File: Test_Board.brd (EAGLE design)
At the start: 50.8 x 50.8 mm, 24 parts, among them U1 Value, U2 Value

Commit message: initial placements done
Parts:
- removed C3: (no value), SparkFun-Capacitors:0603
- removed D1: 3A/40V/500mV, SparkFun-DiscreteSemi:SMA-DIODE
- added C11: 330uF, brick-capacitor-UCM1H331MNL1GS:CAPAE1030X1050N
- added J1, J2, J3: (no value), SparkFun-Connectors:2X4
- added JP1, JP2: JUMPER-SMT_2_NO_NO-SILK, SparkFun-Jumpers:SMT-JUMPER_2_NO_NO-SILK
- added U$4: SWITCHMODE_SCHOTTKY, PowerComponents:DPAK-3
- moved R3 82.6 mm to (31.1, 22.9), turned to 270 degrees
- moved C10 77.0 mm to (27.9, 19.6), turned to 180 degrees
- moved C7 73.1 mm to (34.9, 41.9), turned to 270 degrees
- moved Q1 73.0 mm to (45.1, 40.6), turned to 270 degrees
- moved C5 67.0 mm to (31.1, 16.5), turned to 270 degrees
- moved RSEN 65.4 mm to (38.7, 50.8)
- moved L2 65.3 mm to (42.5, 17.1), turned to 270 degrees
- moved C8 64.8 mm to (24.1, 43.4), turned to 270 degrees
- moved C6 64.3 mm to (34.9, 4.45)
- moved C4 63.7 mm to (26.8, 43.4), turned to 270 degrees
- moved RFB2 60.6 mm to (26.7, 15.9), turned to 90 degrees
- moved U2 48.9 mm to (6.99, 37.5)
- moved C9 47.6 mm to (14.6, 45.3), turned to 90 degrees
- moved C2 44.7 mm to (5.71, 40.6), turned to 180 degrees
- moved U$2 44.4 mm to (10.2, 24.8), turned to 180 degrees
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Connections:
- new net N$14: JP2.2, Q1.1, Q1.2, Q1.3, RSEN.2
- net +12V: now also C11.+; no longer C3.1
- net +12V_A: now also J1.1, J1.3, J1.5, J1.7
- net +12V_B: now also J2.1, J2.3, J2.5, J2.7
- net +48V: now also J3.1, J3.3, J3.5, J3.7
- net 12V_GND: now also C11.-, J1.2, J1.4, J1.6, J1.8, J2.2, J2.4, J2.6, J2.8; no longer C3.2
- net GND: now also J3.2, J3.4, J3.6, J3.8, U$4.P$1, U$4.P$3; no longer D1.A
- net N$1: now also JP1.2, JP2.1; no longer Q1.1, Q1.2, Q1.3, RSEN.2
- net N$11: now also JP1.1, U$4.P$4; no longer D1.C
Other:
- board size 50.8 x 50.8 mm -> 63.5 x 57.1 mm

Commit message: finished routing, but dont have senior design DRC on my PC to check
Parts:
- removed C6: 100uF, SparkFun-Capacitors:EIA7343
- added C3: 150uF, PowerComponents:CTAN(7.30_4.30MM)
- added J4: (no value), SparkFun-Connectors:2X4
- moved RADJ 3.81 mm to (15.9, 45.3)
- moved U$3 3.81 mm to (15.9, 40.6)
- moved C9 3.81 mm to (18.4, 45.3)
- moved JP2 3.24 mm to (24.1, 39.4), turned to 0 degrees
- moved RT 2.54 mm to (12.2, 45.3)
- moved J3 2.54 mm to (21.6, 52.7)
- moved RFB1 1.91 mm to (16.5, 36.2)
- moved JP1 1.65 mm to (20.3, 37.7)
- moved U$4 1.27 mm to (39.4, 30.5)
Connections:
- removed net 12V_GND: C11.-, J1.2, J1.4, J1.6, J1.8, J2.2, J2.4, J2.6, J2.8
- net +12V: now also J4.1, J4.3, J4.5, J4.7
- net +5V: now also C3.+; no longer C6.A
- net GND: now also C11.-, C3.-, J1.2, J1.4, J1.6, J1.8, J2.2, J2.4, J2.6, J2.8, J4.2, J4.4, J4.6, J4.8; no longer C6.C
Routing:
- net N$11: track 0.00 -> 53.2 mm
- net N$16: track 0.00 -> 34.7 mm
- net N$14: track 0.00 -> 31.5 mm, vias 0 -> 2
- net +12V: track 0.00 -> 31.5 mm, vias 0 -> 2
- net GND: track 0.00 -> 27.5 mm, vias 0 -> 5
- net N$4: track 0.00 -> 24.6 mm
- net +48V: track 0.00 -> 14.9 mm
- net N$13: track 0.00 -> 11.2 mm
- net N$10: track 0.00 -> 10.7 mm
- net N$12: track 0.00 -> 6.65 mm
- net N$1: track 0.00 -> 6.51 mm
- net N$15: track 0.00 -> 5.60 mm
- net N$9: track 0.00 -> 4.70 mm
- net N$5: track 0.00 -> 4.70 mm
- net N$2: track 0.00 -> 4.44 mm
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- added copper zone on layer 1, net +12V
- added copper zone on layer 1, net +12V_A
- added copper zone on layer 1, net +12V_B
- added copper zone on layer 1, net +48V
- added copper zone on layer 1, net +5V
- added copper zone on layer 16, net GND
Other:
- board text added: "+12V"
- board text added: "+48V"
- board text added: "12V Out"
- board text added: "12V_A"
- board text added: "12V_B"
- board text added: "GND"

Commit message: finished routing. Need DRC
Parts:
- added J5: (no value), SparkFun-Connectors:1X04_NO_SILK
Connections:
- net +5V: now also J5.3, J5.4
- net GND: now also J5.1, J5.2
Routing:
- net GND: track 27.5 -> 28.2 mm, vias 5 -> 6
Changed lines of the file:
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@@
 <attribute name="VALUE" x="0.635" y="8.763" size="0.6096" layer="27" font="vector" ratio="20" rot="R180"/>
+</element>
+<element name="J5" library="SparkFun-Connectors" library_urn="urn:adsk.eagle:library:513" package="1X04_NO_SILK" package3d_urn="urn:adsk.eagle:package:38094/1" value="" x="40.005" y="2.54" smashed="yes">
+<attribute name="NAME" x="38.735" y="3.937" size="0.6096" layer="25" font="vector" ratio="20"/>
+<attribute name="PROD_ID" value="CONN-09696" x="40.005" y="2.54" size="1.778" layer="27" display="off"/>
+<attribute name="VALUE" x="38.735" y="0.508" size="0.6096" layer="27" font="vector" ratio="20"/>
 </element>
 </elements>
@@
 <contactref element="J4" pad="6"/>
 <contactref element="J4" pad="4"/>
-<wire x1="17.36" y1="36.195" x2="15.875" y2="40.64" width="0" layer="19" extent="1-1"/>
+<contactref element="J5" pad="1"/>
+<contactref element="J5" pad="2"/>
+<wire x1="15.875" y1="40.64" x2="15.875" y2="40.005" width="0.508" layer="1"/>
+<via x="15.875" y="40.005" extent="1-16" drill="0.35"/>
 </signal>
 <signal name="+5V">
@@
 <vertex x="31.75" y="7.62"/>
 </polygon>
+<contactref element="J5" pad="3"/>
+<contactref element="J5" pad="4"/>
 </signal>
 <signal name="+48V">

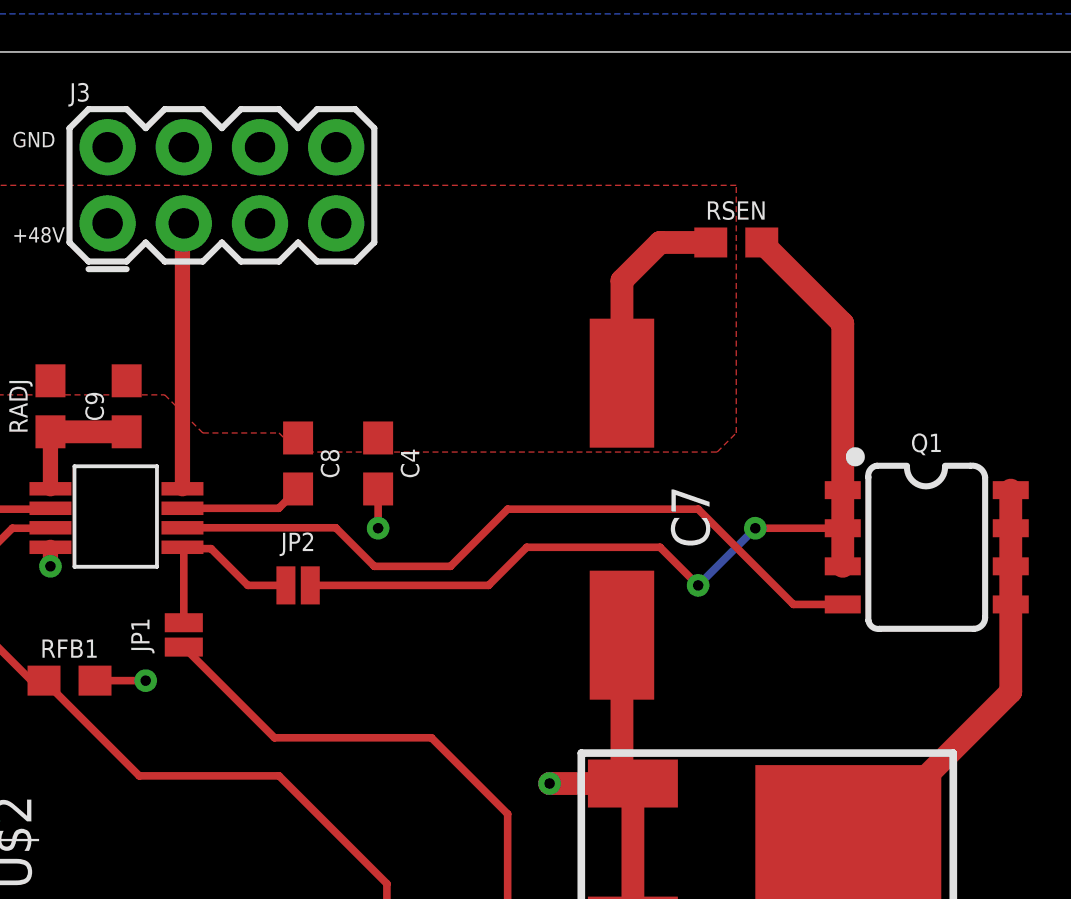
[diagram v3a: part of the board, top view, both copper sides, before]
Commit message: added sense resistor
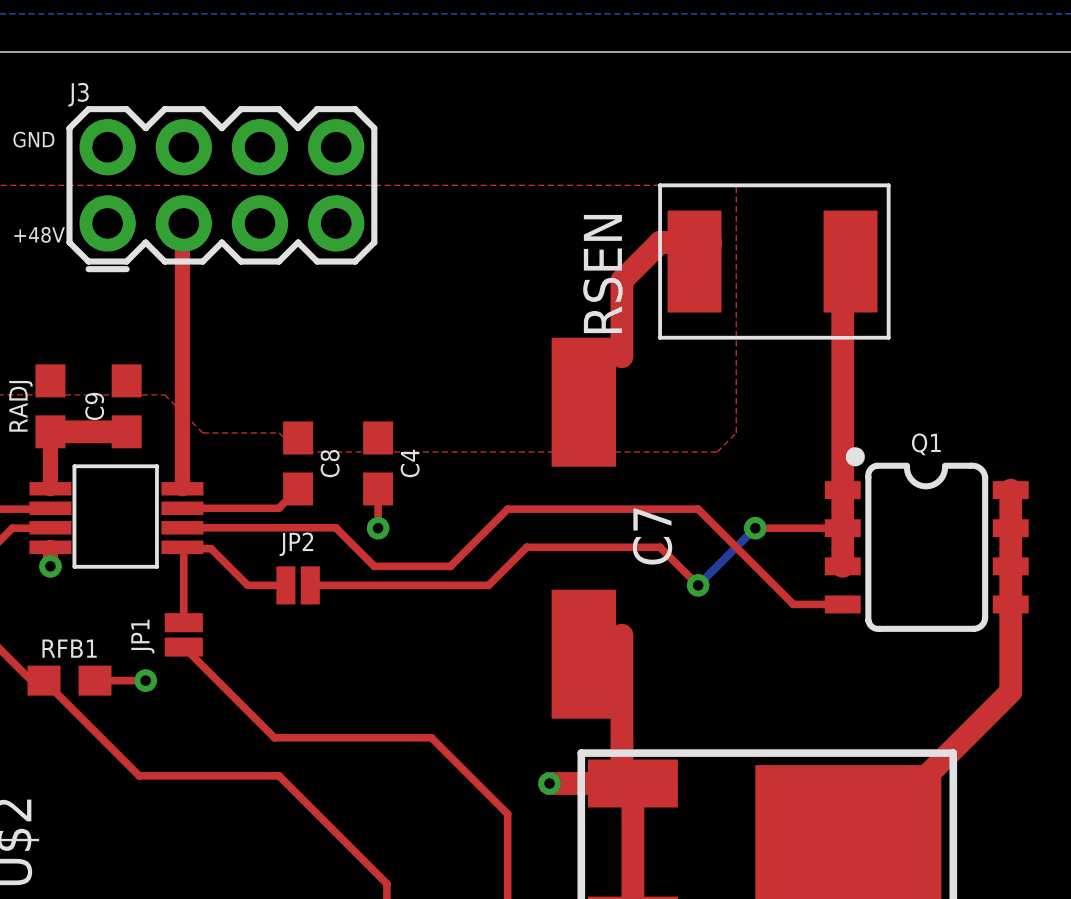
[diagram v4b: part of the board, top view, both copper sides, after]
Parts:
- RSEN: device SparkFun-Resistors:0603 -> INA4181A4:CSS2H-2512
- moved RSEN 3.86 mm to (42.5, 50.2), turned to 90 degrees
- moved C7 1.42 mm to (33.7, 41.3)
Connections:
- net N$1 renamed ISEN
- net +48V: now also RSEN.2; no longer RSEN.1
- net N$14: now also RSEN.1; no longer RSEN.2
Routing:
- net N$14: track 31.5 -> 29.9 mm
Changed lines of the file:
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@@
 <?xml version="1.0" encoding="utf-8"?>
 <!DOCTYPE eagle SYSTEM "eagle.dtd">
-<eagle version="9.5.0">
+<eagle version="9.6.2">
 <drawing>
 <settings>
@@
 <attribute name="VALUE" x="30.353" y="16.51" size="0.6096" layer="27" font="vector" ratio="20" rot="R270" align="top-center"/>
 </element>
-<element name="C7" library="brick-capacitor-UCM1H331MNL1GS" package="CAPAE1030X1050N" package3d_urn="urn:adsk.eagle:package:24202090/2" value="47uF" x="34.925" y="41.91" smashed="yes" rot="R270">
-<attribute name="ARROW_PART_NUMBER" value="UCM1H331MNL1GS" x="6.985" y="5.08" size="1.778" layer="27" rot="R270" display="off"/>
-<attribute name="ARROW_PRICE-STOCK" value="https://www.arrow.com/en/products/ucm1h331mnl1gs/nichicon" x="6.985" y="5.08" size="1.778" layer="27" rot="R270" display="off"/>
-<attribute name="DESCRIPTION" value="Nichicon 330uF 50 V Aluminium Electrolytic Capacitor SMD, CM Series 2000h 10 (Dia.) x 10mm" x="6.985" y="5.08" size="1.778" layer="27" rot="R270" display="off"/>
-<attribute name="HEIGHT" value="10.5mm" x="6.985" y="5.08" size="1.778" layer="27" rot="R270" display="off"/>
-<attribute name="MANUFACTURER_NAME" value="Nichicon" x="6.985" y="5.08" size="1.778" layer="27" rot="R270" display="off"/>
-<attribute name="MANUFACTURER_PART_NUMBER" value="UCM1H331MNL1GS" x="6.985" y="5.08" size="1.778" layer="27" rot="R270" display="off"/>
-<attribute name="MOUSER_PART_NUMBER" value="647-UCM1H331MNL1GS" x="6.985" y="5.08" size="1.778" layer="27" rot="R270" display="off"/>
-<attribute name="MOUSER_PRICE-STOCK" value="https://www.mouser.co.uk/ProductDetail/Nichicon/UCM1H331MNL1GS?qs=DSgADHjnLTkTovFLdbC%252BNg%3D%3D" x="6.985" y="5.08" size="1.778" layer="27" rot="R270" display="off"/>
-<attribute name="NAME" x="37.211" y="41.656" size="1.27" layer="25" rot="R270" align="center"/>
-<attribute name="VALUE" x="32.385" y="41.91" size="1.27" layer="27" rot="R270" align="center"/>
+<element name="C7" library="brick-capacitor-UCM1H331MNL1GS" package="CAPAE1030X1050N" package3d_urn="urn:adsk.eagle:package:24202090/2" value="47uF" x="33.655" y="41.275" smashed="yes" rot="R270">
+<attribute name="ARROW_PART_NUMBER" value="UCM1H331MNL1GS" x="5.715" y="4.445" size="1.778" layer="27" rot="R270" display="off"/>
+<attribute name="ARROW_PRICE-STOCK" value="https://www.arrow.com/en/products/ucm1h331mnl1gs/nichicon" x="5.715" y="4.445" size="1.778" layer="27" rot="R270" display="off"/>
+<attribute name="DESCRIPTION" value="Nichicon 330uF 50 V Aluminium Electrolytic Capacitor SMD, CM Series 2000h 10 (Dia.) x 10mm" x="5.715" y="4.445" size="1.778" layer="27" rot="R270" display="off"/>
+<attribute name="HEIGHT" value="10.5mm" x="5.715" y="4.445" size="1.778" layer="27" rot="R270" display="off"/>
+<attribute name="MANUFACTURER_NAME" value="Nichicon" x="5.715" y="4.445" size="1.778" layer="27" rot="R270" display="off"/>
+<attribute name="MANUFACTURER_PART_NUMBER" value="UCM1H331MNL1GS" x="5.715" y="4.445" size="1.778" layer="27" rot="R270" display="off"/>
+<attribute name="MOUSER_PART_NUMBER" value="647-UCM1H331MNL1GS" x="5.715" y="4.445" size="1.778" layer="27" rot="R270" display="off"/>
+<attribute name="MOUSER_PRICE-STOCK" value="https://www.mouser.co.uk/ProductDetail/Nichicon/UCM1H331MNL1GS?qs=DSgADHjnLTkTovFLdbC%252BNg%3D%3D" x="5.715" y="4.445" size="1.778" layer="27" rot="R270" display="off"/>
+<attribute name="NAME" x="35.941" y="41.021" size="1.27" layer="25" rot="R270" align="center"/>
+<attribute name="VALUE" x="31.115" y="41.275" size="1.27" layer="27" rot="R270" align="center"/>
 </element>
 <element name="C8" library="SparkFun-Capacitors" library_urn="urn:adsk.eagle:library:510" package="0603" package3d_urn="urn:adsk.eagle:package:37414/1" value="0.47uF" x="24.13" y="43.434" smashed="yes" rot="R270">
@@
 <attribute name="PROD_ID" value=" " x="77.47" y="38.735" size="1.778" layer="27" rot="R90" display="off"/>
 <attribute name="VALUE" x="27.432" y="15.875" size="0.6096" layer="27" font="vector" ratio="20" rot="R90" align="top-center"/>
-</element>
-<element name="RSEN" library="SparkFun-Resistors" library_urn="urn:adsk.eagle:library:532" package="0603" package3d_urn="urn:adsk.eagle:package:39650/1" value="0.01" x="38.735" y="50.8" smashed="yes">
-<attribute name="NAME" x="38.735" y="51.562" size="0.6096" layer="25" font="vector" ratio="20" align="bottom-center"/>
-<attribute name="PROD_ID" value=" " x="65.405" y="0" size="1.778" layer="27" display="off"/>
-<attribute name="VALUE" x="38.735" y="50.038" size="0.6096" layer="27" font="vector" ratio="20" align="top-center"/>
 </element>
 <element name="RT" library="SparkFun-Resistors" library_urn="urn:adsk.eagle:library:532" package="0603" package3d_urn="urn:adsk.eagle:package:39650/1" value="77.7k" x="12.192" y="45.339" smashed="yes" rot="R90">
@@
 <attribute name="PROD_ID" value="CONN-09696" x="40.005" y="2.54" size="1.778" layer="27" display="off"/>
 <attribute name="VALUE" x="38.735" y="0.508" size="0.6096" layer="27" font="vector" ratio="20"/>
+</element>
+<element name="RSEN" library="INA4181A4" package="CSS2H-2512" value="0.01" x="42.545" y="50.165" smashed="yes" rot="R90">
+<attribute name="NAME" x="34.925" y="47.625" size="1.27" layer="25" rot="R90"/>
+<attribute name="VALUE" x="46.355" y="47.625" size="1.27" layer="27" rot="R90"/>
 </element>
 </elements>
@@
 <contactref element="RT" pad="2"/>
 <contactref element="RADJ" pad="2"/>
-<contactref element="RSEN" pad="1"/>
 <contactref element="C7" pad="+"/>
 <contactref element="C8" pad="1"/>
@@
 <wire x1="20.275" y1="42.59" x2="20.275" y2="51.39" width="0.508" layer="1"/>
 <wire x1="20.275" y1="51.39" x2="20.32" y2="51.435" width="0.508" layer="1"/>
+<contactref element="RSEN" pad="2"/>
 </signal>
 <signal name="N$3">
@@
 <wire x1="15.66" y1="36.195" x2="18.835" y2="33.02" width="0.254" layer="1"/>
 </signal>
-<signal name="N$1">
+<signal name="ISEN">
 <contactref element="U$3" pad="5"/>
-<contactref element="JP1" pad="2"/>
 <contactref element="JP2" pad="1"/>
-<wire x1="20.329425" y1="38.1" x2="20.328284375" y2="38.103075" width="0.254" layer="1"/>
-<wire x1="20.328284375" y1="38.103075" x2="20.32" y2="38.1254" width="0.254" layer="1"/>
-<wire x1="20.32" y1="38.1254" x2="20.3454" y2="38.1" width="0.254" layer="1"/>
 <wire x1="20.275" y1="40.64" x2="20.32" y2="40.595" width="0.254" layer="1"/>
 <wire x1="20.32" y1="40.595" x2="20.32" y2="38.1254" width="0.254" layer="1"/>
@@
 <wire x1="23.7236" y1="39.37" x2="22.4536" y2="39.37" width="0.254" layer="1"/>
 <wire x1="22.4536" y1="39.37" x2="21.2286" y2="40.595" width="0.254" layer="1"/>
+<contactref element="JP1" pad="2"/>
+<wire x1="20.32" y1="38.1254" x2="20.275" y2="40.64" width="0" layer="19" extent="1-1"/>
 </signal>
 <signal name="N$14">
 <contactref element="JP2" pad="2"/>
-<contactref element="RSEN" pad="2"/>
 <contactref element="Q1" pad="1"/>
 <contactref element="Q1" pad="2"/>
@@
 <wire x1="42.285" y1="42.545" x2="42.285" y2="41.275" width="0.762" layer="1"/>
 <wire x1="42.285" y1="41.275" x2="42.285" y2="40.005" width="0.762" layer="1"/>
-<wire x1="42.285" y1="42.545" x2="42.285" y2="48.1" width="0.762" layer="1"/>
-<wire x1="42.285" y1="48.1" x2="39.585" y2="50.8" width="0.762" layer="1"/>
 <wire x1="24.5364" y1="39.37" x2="30.48" y2="39.37" width="0.254" layer="1"/>
 <wire x1="30.48" y1="39.37" x2="31.75" y2="40.64" width="0.254" layer="1"/>
@@
 <via x="39.37" y="41.275" extent="1-16" drill="0.35"/>
 <wire x1="39.37" y1="41.275" x2="42.285" y2="41.275" width="0.254" layer="1"/>
+<contactref element="RSEN" pad="1"/>
+<wire x1="42.285" y1="49.905" x2="42.545" y2="50.165" width="0.762" layer="1"/>
+<wire x1="42.285" y1="42.545" x2="42.285" y2="49.905" width="0.762" layer="1"/>
 </signal>
 </signals>

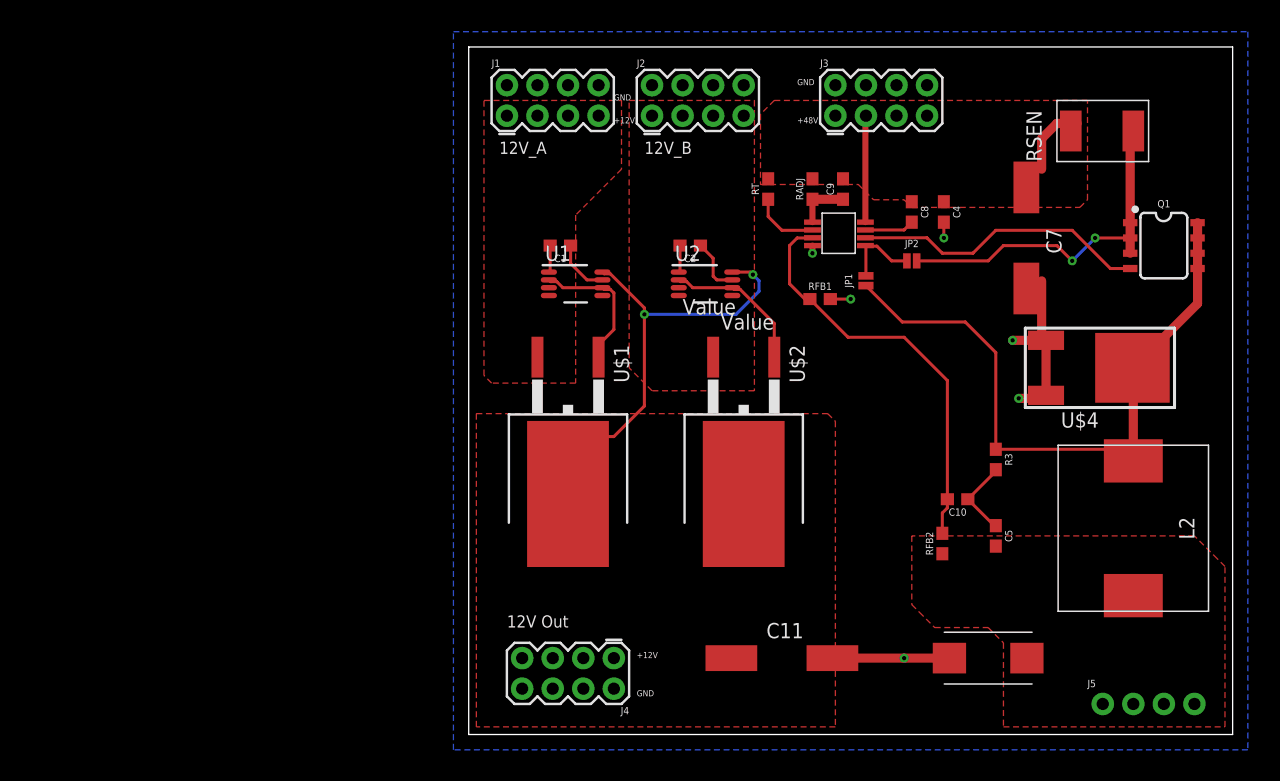
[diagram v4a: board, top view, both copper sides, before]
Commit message: rerouted buck converter, trying to mitigate distance and also follow the recommended layout
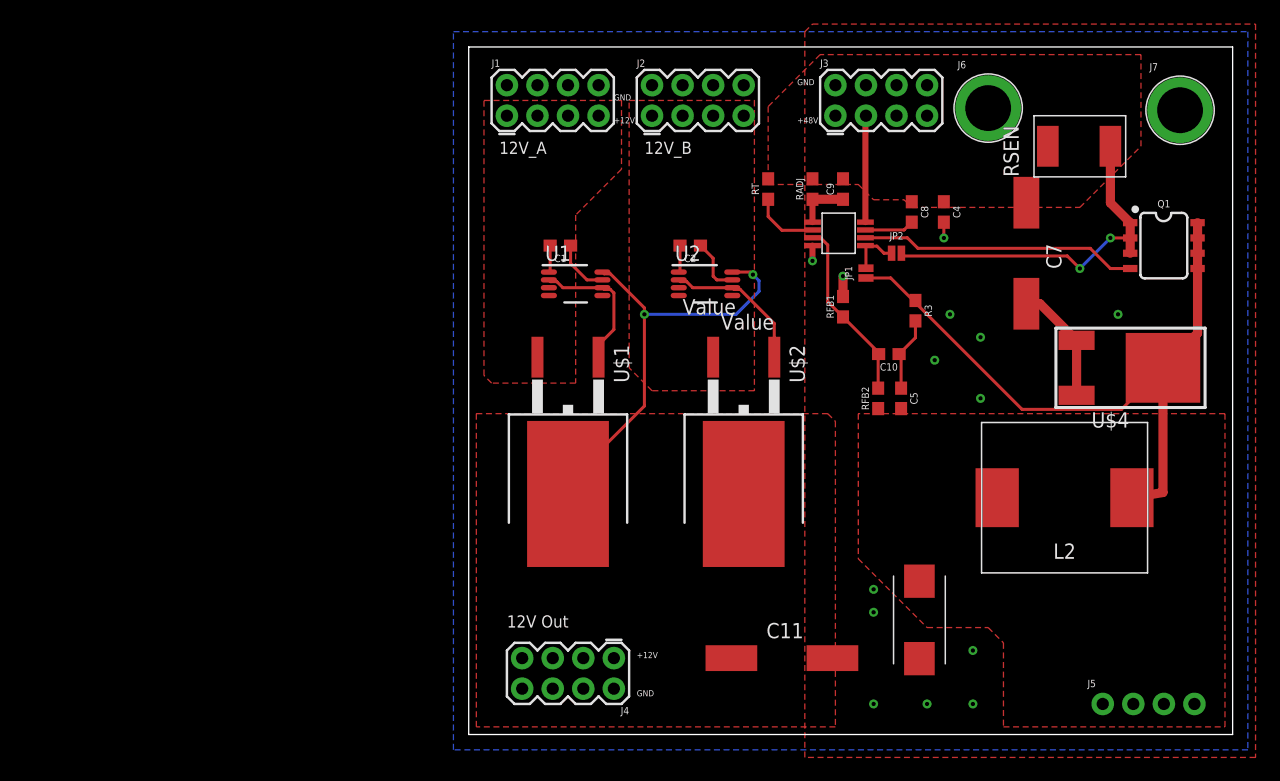
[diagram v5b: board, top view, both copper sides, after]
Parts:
- added J6, J7: (no value), SparkFun-Connectors:BANANA_CONN
- moved R3 14.1 mm to (24.4, 35.2)
- moved C5 13.9 mm to (23.2, 27.9)
- moved C10 13.4 mm to (22.2, 31.6)
- moved RFB2 13.2 mm to (21.3, 27.9)
- moved C3 6.54 mm to (24.8, 9.53), turned to 270 degrees
- moved L2 6.25 mm to (36.8, 19.7), turned to 180 degrees
- moved U$4 2.54 mm to (41.9, 30.5)
- moved RSEN 2.29 mm to (40.6, 48.9)
- moved RFB1 2.01 mm to (18.4, 35.6), turned to 90 degrees
- moved JP2 1.42 mm to (22.9, 40.0)
- moved C7 1.27 mm to (33.7, 40.0)
- moved JP1 0.63 mm to (20.3, 38.4)
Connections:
- net N$15 renamed RT
- net N$16 renamed FB
- net N$3 renamed VCC
- net N$4 renamed GATE
- net +48V: now also J6.P$1
- net GND: now also J7.P$1
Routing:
- net FB: track 34.7 -> 15.2 mm
- net GND: track 28.2 -> 14.3 mm, vias 6 -> 14
- net +48V: track 14.9 -> 8.86 mm
- net +12V: track 31.5 -> 36.5 mm
- net N$11: track 53.2 -> 57.1 mm
- net ISEN: track 6.44 -> 4.28 mm
- net GATE: track 24.6 -> 23.1 mm
- net N$13: track 11.2 -> 12.2 mm
- net N$10: track 10.7 -> 11.7 mm
- added copper zone on layer 1, net GND
